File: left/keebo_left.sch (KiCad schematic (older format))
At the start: 58 parts, among them SW1 SW_Push, SW10 SW_Push, SW11 SW_Push, SW12 SW_Push, SW13 SW_Push, SW14 SW_Push, SW17 SW_Push, SW18 SW_Push, SW19 SW_Push, SW2 SW_Push, SW20 SW_Push, SW21 SW_Push, SW22 SW_Push, SW25 SW_Push, SW26 SW_Push, SW27 SW_Push, SW28 SW_Push, SW29 SW_Push, SW3 SW_Push, SW30 SW_Push, SW34 SW_Push, SW35 SW_Push, SW36 SW_Push, SW4 SW_Push, SW5 SW_Push, SW6 SW_Push, SW7 SW_Push, SW9 SW_Push, U1 nRF24L01_module, U2 keyplus_mini

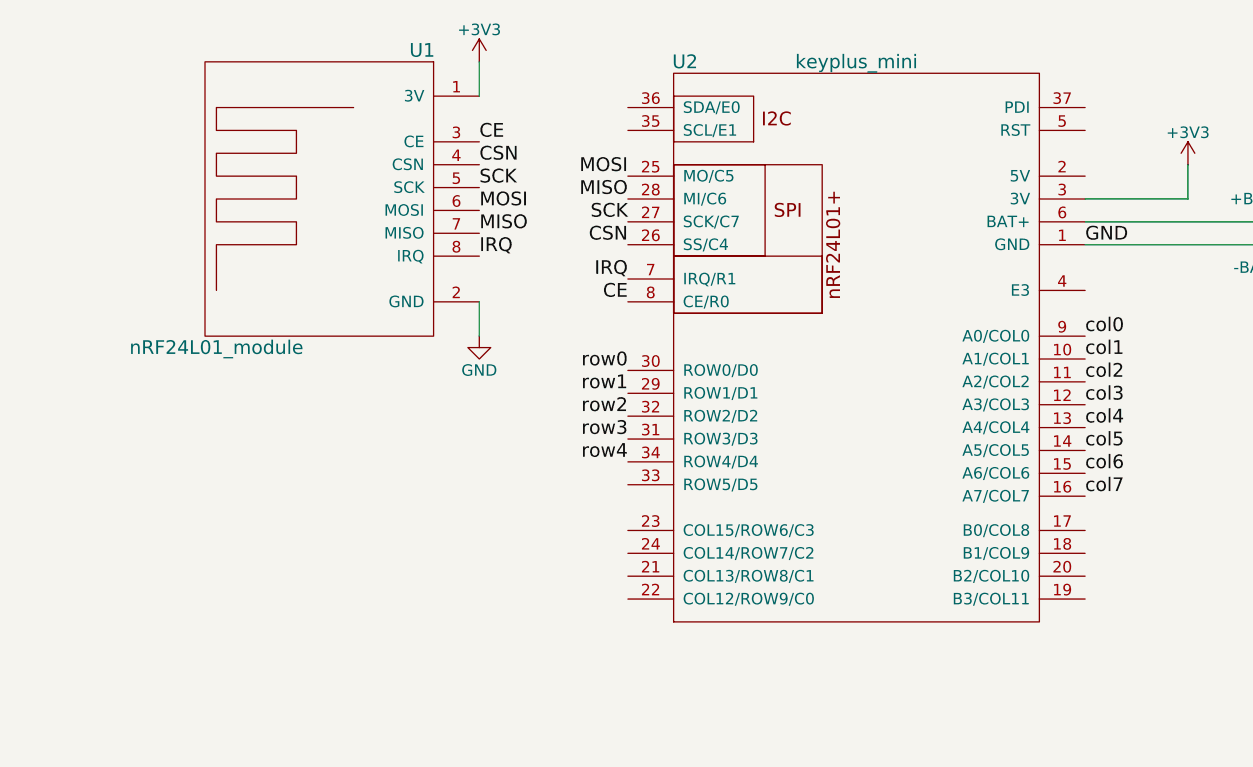
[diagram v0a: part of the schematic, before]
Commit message: Make dependencies use relative path
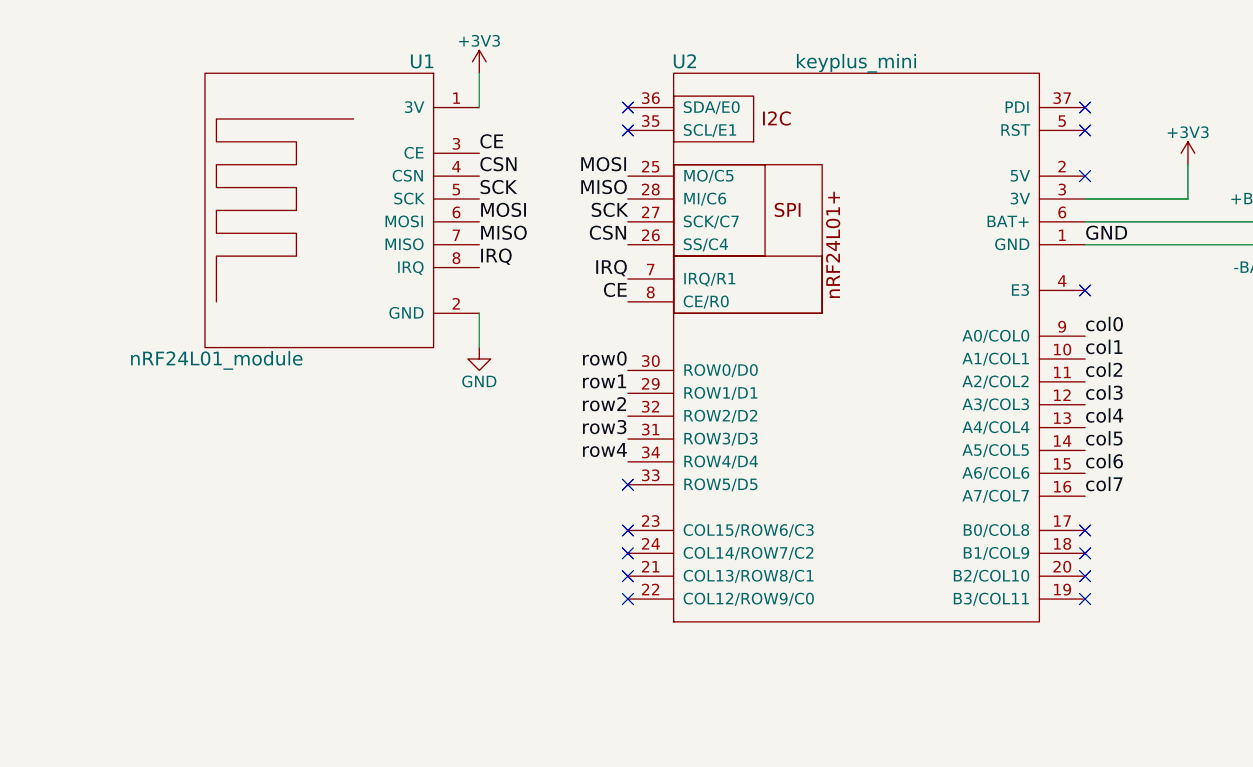
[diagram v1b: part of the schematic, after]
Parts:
- U1: footprint nordic:NRF24L01-Module-SMD-TH -> Pin_Headers:Pin_Header_Straight_1x08_Pitch2.54mm
- U2: footprint keyplus:keyplus_mini_v3 -> Pin_Headers:Pin_Header_Straight_1x13_Pitch2.54mm
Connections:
- no-connect marks 0 -> 15
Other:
- moved on the sheet: U1
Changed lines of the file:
@@
 F 0 "U2" H 3050 3650 60  0000 C CNN
 F 1 "keyplus_mini" H 3800 3650 60  0000 C CNN
-F 2 "keyplus:keyplus_mini_v3" H 3800 2400 60  0001 C CNN
+F 2 "Pin_Headers:Pin_Header_Straight_1x13_Pitch2.54mm" H 3800 2400 60  0001 C CNN
 F 3 "" H 3800 2400 60  0001 C CNN
 	1    3800 2400
@@
 L nRF24L01_module U1
 U 1 1 5ADCD4B6
-P 1450 1750
-F 0 "U1" H 1000 2400 60  0000 C CNN
-F 1 "nRF24L01_module" H 1900 1100 60  0000 C CNN
-F 2 "nordic:NRF24L01-Module-SMD-TH" H 1450 1700 60  0001 C CNN
-F 3 "" H 1450 1700 60  0001 C CNN
-	1    1450 1750
+P 1450 1800
+F 0 "U1" H 1000 2450 60  0000 C CNN
+F 1 "nRF24L01_module" H 1900 1150 60  0000 C CNN
+F 2 "Pin_Headers:Pin_Header_Straight_1x08_Pitch2.54mm" H 1450 1750 60  0001 C CNN
+F 3 "" H 1450 1750 60  0001 C CNN
+	1    1450 1800
 	-1   0    0    -1
 $EndComp
@@
 Connection ~ 750  7450
 Connection ~ 150  7400
-Text Label 2800 2500 2    60   ~ 0
-row0
-Text Label 2800 2600 2    60   ~ 0
-row1
-Text Label 2800 2700 2    60   ~ 0
-row2
-Text Label 2800 2800 2    60   ~ 0
-row3
-Text Label 2800 2900 2    60   ~ 0
-row4
-Text Label 4800 2350 0    60   ~ 0
-col0
-Text Label 4800 2450 0    60   ~ 0
-col1
-Text Label 4800 2550 0    60   ~ 0
-col2
-Text Label 4800 2650 0    60   ~ 0
-col3
-Text Label 4800 2750 0    60   ~ 0
-col4
-Text Label 4800 2850 0    60   ~ 0
-col5
-Text Label 4800 2950 0    60   ~ 0
-col6
-Text Label 4800 3050 0    60   ~ 0
-col7
 Text Label 2800 1650 2    60   ~ 0
 MOSI
@@
 Text Label 2800 2200 2    60   ~ 0
 CE
-Text Label 2150 2000 0    60   ~ 0
+Text Label 2150 2050 0    60   ~ 0
 IRQ
-Text Label 2150 1900 0    60   ~ 0
+Text Label 2150 1950 0    60   ~ 0
 MISO
-Text Label 2150 1800 0    60   ~ 0
+Text Label 2150 1850 0    60   ~ 0
 MOSI
-Text Label 2150 1700 0    60   ~ 0
+Text Label 2150 1750 0    60   ~ 0
 SCK
-Text Label 2150 1600 0    60   ~ 0
+Text Label 2150 1650 0    60   ~ 0
 CSN
-Text Label 2150 1500 0    60   ~ 0
+Text Label 2150 1550 0    60   ~ 0
 CE
 $Comp
@@
 $EndComp
 Wire Wire Line
-	2150 2200 2150 2350
+	2150 2250 2150 2400
 $Comp
 L GND #PWR03
 U 1 1 5ADE070A
-P 2150 2350
-F 0 "#PWR03" H 2150 2100 50  0001 C CNN
-F 1 "GND" H 2150 2200 50  0000 C CNN
-F 2 "" H 2150 2350 50  0001 C CNN
-F 3 "" H 2150 2350 50  0001 C CNN
-	1    2150 2350
-	1    0    0    -1
-$EndComp
-Wire Wire Line
-	2150 1300 2150 1150
+P 2150 2400
+F 0 "#PWR03" H 2150 2150 50  0001 C CNN
+F 1 "GND" H 2150 2250 50  0000 C CNN
+F 2 "" H 2150 2400 50  0001 C CNN
+F 3 "" H 2150 2400 50  0001 C CNN
+	1    2150 2400
+	1    0    0    -1
+$EndComp
+Wire Wire Line
+	2150 1350 2150 1200
 $Comp
 L +3V3 #PWR04
 U 1 1 5ADE0A2C
-P 2150 1150
-F 0 "#PWR04" H 2150 1000 50  0001 C CNN
-F 1 "+3V3" H 2150 1290 50  0000 C CNN
-F 2 "" H 2150 1150 50  0001 C CNN
-F 3 "" H 2150 1150 50  0001 C CNN
-	1    2150 1150
+P 2150 1200
+F 0 "#PWR04" H 2150 1050 50  0001 C CNN
+F 1 "+3V3" H 2150 1340 50  0000 C CNN
+F 2 "" H 2150 1200 50  0001 C CNN
+F 3 "" H 2150 1200 50  0001 C CNN
+	1    2150 1200
 	1    0    0    -1
 $EndComp
@@
 Text Label 4800 1950 0    60   ~ 0
 GND
+NoConn ~ 4800 1350
+NoConn ~ 4800 1450
+NoConn ~ 4800 1650
+NoConn ~ 4800 2150
+NoConn ~ 2800 3000
+NoConn ~ 2800 3200
+NoConn ~ 2800 3300
+NoConn ~ 2800 3400
+NoConn ~ 2800 3500
+NoConn ~ 4800 3500
+NoConn ~ 4800 3400
+NoConn ~ 4800 3300
+NoConn ~ 4800 3200
+NoConn ~ 2800 1350
+NoConn ~ 2800 1450
+Text Label 4800 3050 0    60   ~ 0
+col7
+Text Label 4800 2950 0    60   ~ 0
+col6
+Text Label 4800 2850 0    60   ~ 0
+col5
+Text Label 4800 2750 0    60   ~ 0
+col4
+Text Label 4800 2650 0    60   ~ 0
+col3
+Text Label 4800 2550 0    60   ~ 0
+col2
+Text Label 4800 2450 0    60   ~ 0
+col1
+Text Label 4800 2350 0    60   ~ 0
+col0
+Text Label 2800 2500 2    60   ~ 0
+row0
+Text Label 2800 2600 2    60   ~ 0
+row1
+Text Label 2800 2700 2    60   ~ 0
+row2
+Text Label 2800 2800 2    60   ~ 0
+row3
+Text Label 2800 2900 2    60   ~ 0
+row4
 $EndSCHEMATC

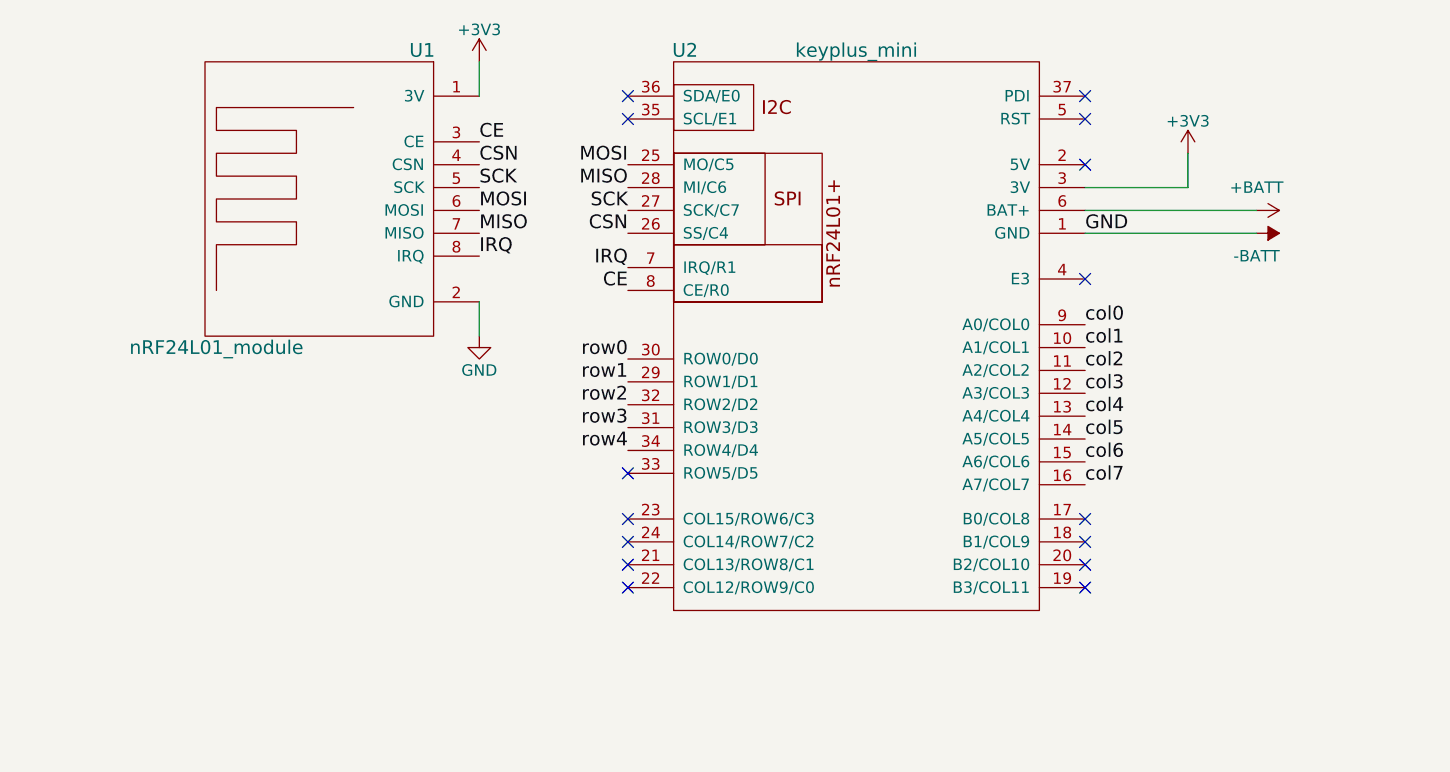
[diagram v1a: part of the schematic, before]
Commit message: Remove separate components
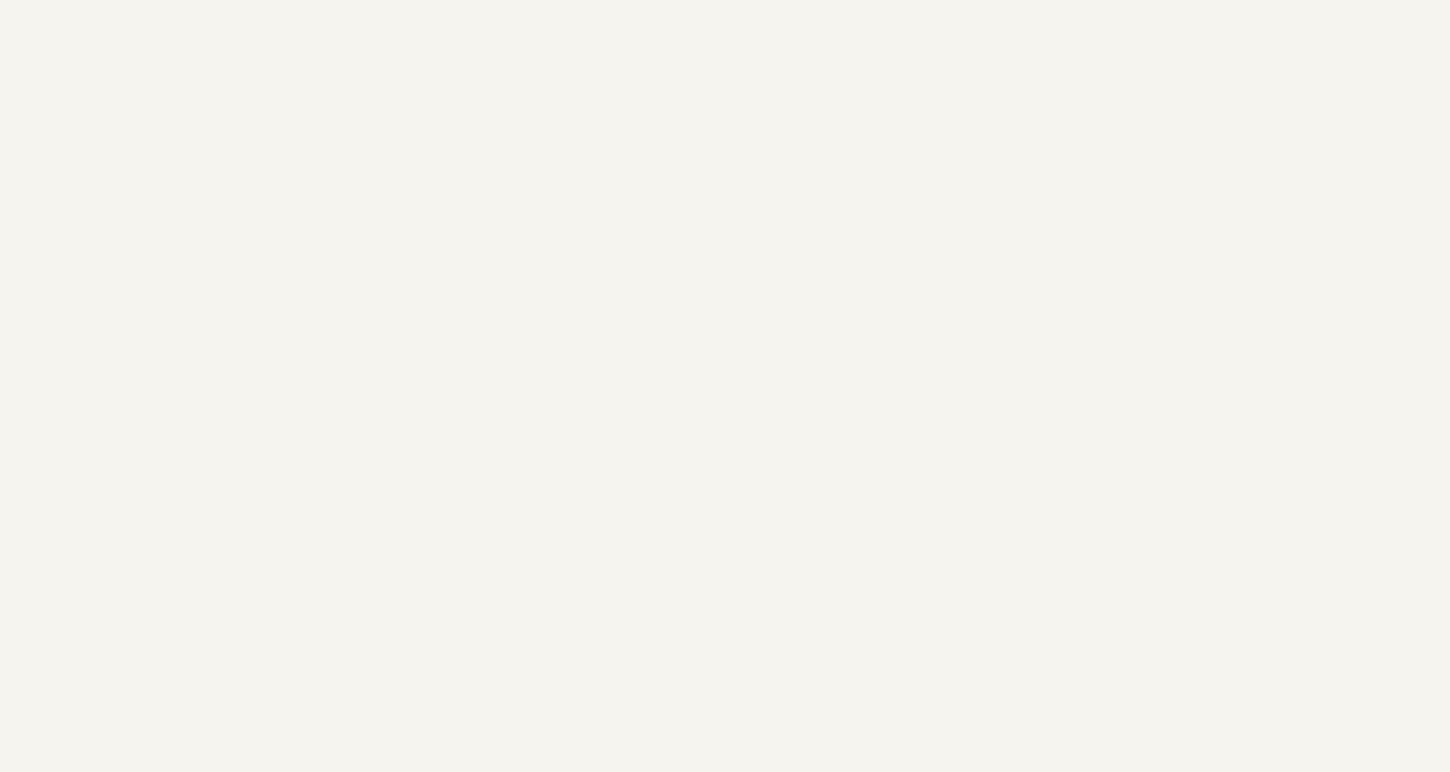
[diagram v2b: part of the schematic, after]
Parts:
- removed U1: nRF24L01_module, Pin_Headers:Pin_Header_Straight_1x08_Pitch2.54mm, symbol nRF24L01_module
- removed U2: keyplus_mini, Pin_Headers:Pin_Header_Straight_1x13_Pitch2.54mm, symbol keyplus_mini
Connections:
- no-connect marks 15 -> 0
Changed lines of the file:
@@
 LIBS:power
 LIBS:switches
-LIBS:keebo_left-cache
 EELAYER 25 0
 EELAYER END
@@
 Comment4 ""
 $EndDescr
-$Comp
-L keyplus_mini U2
-U 1 1 5ADCD481
-P 3800 2400
-F 0 "U2" H 3050 3650 60  0000 C CNN
-F 1 "keyplus_mini" H 3800 3650 60  0000 C CNN
-F 2 "Pin_Headers:Pin_Header_Straight_1x13_Pitch2.54mm" H 3800 2400 60  0001 C CNN
-F 3 "" H 3800 2400 60  0001 C CNN
-	1    3800 2400
-	1    0    0    -1
-$EndComp
-$Comp
-L nRF24L01_module U1
-U 1 1 5ADCD4B6
-P 1450 1800
-F 0 "U1" H 1000 2450 60  0000 C CNN
-F 1 "nRF24L01_module" H 1900 1150 60  0000 C CNN
-F 2 "Pin_Headers:Pin_Header_Straight_1x08_Pitch2.54mm" H 1450 1750 60  0001 C CNN
-F 3 "" H 1450 1750 60  0001 C CNN
-	1    1450 1800
-	-1   0    0    -1
-$EndComp
 $Comp
 L SW_Push SW1
@@
 Connection ~ 750  7450
 Connection ~ 150  7400
-Text Label 2800 1650 2    60   ~ 0
-MOSI
-Text Label 2800 1750 2    60   ~ 0
-MISO
-Text Label 2800 1850 2    60   ~ 0
-SCK
-Text Label 2800 1950 2    60   ~ 0
-CSN
-Text Label 2800 2100 2    60   ~ 0
-IRQ
-Text Label 2800 2200 2    60   ~ 0
-CE
-Text Label 2150 2050 0    60   ~ 0
-IRQ
-Text Label 2150 1950 0    60   ~ 0
-MISO
-Text Label 2150 1850 0    60   ~ 0
-MOSI
-Text Label 2150 1750 0    60   ~ 0
-SCK
-Text Label 2150 1650 0    60   ~ 0
-CSN
-Text Label 2150 1550 0    60   ~ 0
-CE
-$Comp
-L +BATT #PWR01
-U 1 1 5ADDDC9B
-P 5550 1850
-F 0 "#PWR01" H 5550 1700 50  0001 C CNN
-F 1 "+BATT" V 5450 1850 50  0000 C CNN
-F 2 "" H 5550 1850 50  0001 C CNN
-F 3 "" H 5550 1850 50  0001 C CNN
-	1    5550 1850
-	0    1    1    0
-$EndComp
-$Comp
-L -BATT #PWR02
-U 1 1 5ADDDD2F
-P 5550 1950
-F 0 "#PWR02" H 5550 1800 50  0001 C CNN
-F 1 "-BATT" V 5650 1950 50  0000 C CNN
-F 2 "" H 5550 1950 50  0001 C CNN
-F 3 "" H 5550 1950 50  0001 C CNN
-	1    5550 1950
-	0    1    1    0
-$EndComp
-Wire Wire Line
-	2150 2250 2150 2400
-$Comp
-L GND #PWR03
-U 1 1 5ADE070A
-P 2150 2400
-F 0 "#PWR03" H 2150 2150 50  0001 C CNN
-F 1 "GND" H 2150 2250 50  0000 C CNN
-F 2 "" H 2150 2400 50  0001 C CNN
-F 3 "" H 2150 2400 50  0001 C CNN
-	1    2150 2400
-	1    0    0    -1
-$EndComp
-Wire Wire Line
-	2150 1350 2150 1200
-$Comp
-L +3V3 #PWR04
-U 1 1 5ADE0A2C
-P 2150 1200
-F 0 "#PWR04" H 2150 1050 50  0001 C CNN
-F 1 "+3V3" H 2150 1340 50  0000 C CNN
-F 2 "" H 2150 1200 50  0001 C CNN
-F 3 "" H 2150 1200 50  0001 C CNN
-	1    2150 1200
-	1    0    0    -1
-$EndComp
-Wire Wire Line
-	4800 1850 5550 1850
-Wire Wire Line
-	5550 1950 4800 1950
-Wire Wire Line
-	4800 1750 5250 1750
-Wire Wire Line
-	5250 1750 5250 1600
-$Comp
-L +3V3 #PWR05
-U 1 1 5ADE1506
-P 5250 1600
-F 0 "#PWR05" H 5250 1450 50  0001 C CNN
-F 1 "+3V3" H 5250 1740 50  0000 C CNN
-F 2 "" H 5250 1600 50  0001 C CNN
-F 3 "" H 5250 1600 50  0001 C CNN
-	1    5250 1600
-	1    0    0    -1
-$EndComp
 Wire Wire Line
 	750  5950 4500 5950
-Text Label 4800 1950 0    60   ~ 0
-GND
-NoConn ~ 4800 1350
-NoConn ~ 4800 1450
-NoConn ~ 4800 1650
-NoConn ~ 4800 2150
-NoConn ~ 2800 3000
-NoConn ~ 2800 3200
-NoConn ~ 2800 3300
-NoConn ~ 2800 3400
-NoConn ~ 2800 3500
-NoConn ~ 4800 3500
-NoConn ~ 4800 3400
-NoConn ~ 4800 3300
-NoConn ~ 4800 3200
-NoConn ~ 2800 1350
-NoConn ~ 2800 1450
-Text Label 4800 3050 0    60   ~ 0
-col7
-Text Label 4800 2950 0    60   ~ 0
-col6
-Text Label 4800 2850 0    60   ~ 0
-col5
-Text Label 4800 2750 0    60   ~ 0
-col4
-Text Label 4800 2650 0    60   ~ 0
-col3
-Text Label 4800 2550 0    60   ~ 0
-col2
-Text Label 4800 2450 0    60   ~ 0
-col1
-Text Label 4800 2350 0    60   ~ 0
-col0
-Text Label 2800 2500 2    60   ~ 0
-row0
-Text Label 2800 2600 2    60   ~ 0
-row1
-Text Label 2800 2700 2    60   ~ 0
-row2
-Text Label 2800 2800 2    60   ~ 0
-row3
-Text Label 2800 2900 2    60   ~ 0
-row4
 $EndSCHEMATC
